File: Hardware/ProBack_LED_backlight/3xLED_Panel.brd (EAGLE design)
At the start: 48 x 6 mm, 11 parts

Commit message: Update boards and schematic
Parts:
- moved D1 0.05 mm to (12.0, 1.30), turned to 180 degrees
- turned D2 to 180 degrees
- turned D3 to 180 degrees
- turned D4 to 180 degrees
- turned D5 to 180 degrees
- turned D6 to 180 degrees
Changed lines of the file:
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@@
 </autorouter>
 <elements>
-<element name="D1" library="Yuji_LED" package="2835_SMD" value="YUJI_2835_SMD" x="12" y="1.25" smashed="yes">
-<attribute name="NAME" x="14.62" y="0.92" size="0.6096" layer="21"/>
-</element>
-<element name="D2" library="Yuji_LED" package="2835_SMD" value="YUJI_2835_SMD" x="24" y="1.25" smashed="yes">
-<attribute name="NAME" x="26.62" y="1.02" size="0.6096" layer="21"/>
+<element name="D1" library="Yuji_LED" package="2835_SMD" value="YUJI_2835_SMD" x="12" y="1.3" smashed="yes" rot="R180"/>
+<element name="D2" library="Yuji_LED" package="2835_SMD" value="YUJI_2835_SMD" x="24" y="1.25" smashed="yes" rot="R180">
+<attribute name="NAME" x="21.38" y="1.48" size="0.6096" layer="21" rot="R180"/>
 </element>
 <element name="FRAME1" library="SparkFun-Aesthetics" package="CREATIVE_COMMONS" value="FRAME-LEDGER" x="0" y="0" smashed="yes">
@@
 <attribute name="VALUE" x="46.1" y="1.3" size="0.0254" layer="27" rot="R90"/>
 </element>
-<element name="D3" library="Yuji_LED" package="2835_SMD" value="YUJI_2835_SMD" x="36" y="1.25" smashed="yes">
-<attribute name="NAME" x="38.52" y="1.02" size="0.6096" layer="21"/>
+<element name="D3" library="Yuji_LED" package="2835_SMD" value="YUJI_2835_SMD" x="36" y="1.25" smashed="yes" rot="R180">
+<attribute name="NAME" x="33.48" y="1.48" size="0.6096" layer="21" rot="R180"/>
 </element>
-<element name="D4" library="Yuji_LED" package="2835_SMD" value="YUJI_2835_SMD" x="12" y="4.75" smashed="yes"/>
-<element name="D5" library="Yuji_LED" package="2835_SMD" value="YUJI_2835_SMD" x="24" y="4.75" smashed="yes"/>
+<element name="D4" library="Yuji_LED" package="2835_SMD" value="YUJI_2835_SMD" x="12" y="4.75" smashed="yes" rot="R180"/>
+<element name="D5" library="Yuji_LED" package="2835_SMD" value="YUJI_2835_SMD" x="24" y="4.75" smashed="yes" rot="R180"/>
 <element name="+1" library="wirepad" package="2,15/1,0" package3d_urn="urn:adsk.eagle:package:30831/1" value="WIREPAD1,6/0,9" x="1.9" y="4.7" smashed="yes">
 <attribute name="POPULARITY" value="11" x="1.9" y="-3.3" size="1.778" layer="27" display="off"/>
@@
 <attribute name="VALUE" x="46.1" y="5.7" size="0.0254" layer="27"/>
 </element>
-<element name="D6" library="Yuji_LED" package="2835_SMD" value="YUJI_2835_SMD" x="36" y="4.75" smashed="yes"/>
+<element name="D6" library="Yuji_LED" package="2835_SMD" value="YUJI_2835_SMD" x="36" y="4.75" smashed="yes" rot="R180"/>
 </elements>
 <signals>
@@
 <contactref element="D1" pad="CATHODE"/>
 <contactref element="D2" pad="ANODE"/>
-<wire x1="12.95" y1="1.25" x2="22.7" y2="1.25" width="1.27" layer="1"/>
+<wire x1="13.3" y1="1.3" x2="23.05" y2="1.25" width="1.27" layer="1"/>
 </signal>
 <signal name="N$2">
 <contactref element="+" pad="1"/>
 <contactref element="D1" pad="ANODE"/>
-<wire x1="1.9" y1="1.3" x2="10.65" y2="1.3" width="1.27" layer="1"/>
-<wire x1="10.65" y1="1.3" x2="10.7" y2="1.25" width="1.27" layer="1"/>
+<wire x1="1.9" y1="1.3" x2="11.05" y2="1.3" width="1.27" layer="1"/>
 </signal>
 <signal name="N$3">
 <contactref element="D2" pad="CATHODE"/>
 <contactref element="D3" pad="ANODE"/>
-<wire x1="24.95" y1="1.25" x2="34.7" y2="1.25" width="1.27" layer="1"/>
+<wire x1="35.05" y1="1.25" x2="25.3" y2="1.25" width="1.27" layer="1"/>
 </signal>
 <signal name="N$4">
 <contactref element="D3" pad="CATHODE"/>
 <contactref element="-" pad="1"/>
-<wire x1="36.95" y1="1.25" x2="46.05" y2="1.25" width="1.27" layer="1"/>
+<wire x1="37.3" y1="1.25" x2="46.05" y2="1.25" width="1.27" layer="1"/>
 <wire x1="46.05" y1="1.25" x2="46.1" y2="1.3" width="1.27" layer="1"/>
 </signal>
@@
 <contactref element="D4" pad="CATHODE"/>
 <contactref element="D5" pad="ANODE"/>
-<wire x1="12.95" y1="4.75" x2="22.7" y2="4.75" width="1.27" layer="1"/>
+<wire x1="13.3" y1="4.75" x2="23.05" y2="4.75" width="1.27" layer="1"/>
 </signal>
 <signal name="N$6">
@@
 <contactref element="D4" pad="ANODE"/>
 <wire x1="1.9" y1="4.7" x2="1.95" y2="4.75" width="1.27" layer="1"/>
-<wire x1="1.95" y1="4.75" x2="10.7" y2="4.75" width="1.27" layer="1"/>
+<wire x1="1.95" y1="4.75" x2="11.05" y2="4.75" width="1.27" layer="1"/>
 </signal>
 <signal name="N$7">
 <contactref element="D5" pad="CATHODE"/>
 <contactref element="D6" pad="ANODE"/>
-<wire x1="24.95" y1="4.75" x2="34.7" y2="4.75" width="1.27" layer="1"/>
+<wire x1="25.3" y1="4.75" x2="35.05" y2="4.75" width="1.27" layer="1"/>
 </signal>
 <signal name="N$8">
 <contactref element="D6" pad="CATHODE"/>
 <contactref element="-1" pad="1"/>
-<wire x1="36.95" y1="4.75" x2="46.05" y2="4.75" width="1.27" layer="1"/>
+<wire x1="37.3" y1="4.75" x2="46.05" y2="4.75" width="1.27" layer="1"/>
 <wire x1="46.05" y1="4.75" x2="46.1" y2="4.7" width="1.27" layer="1"/>
 </signal>

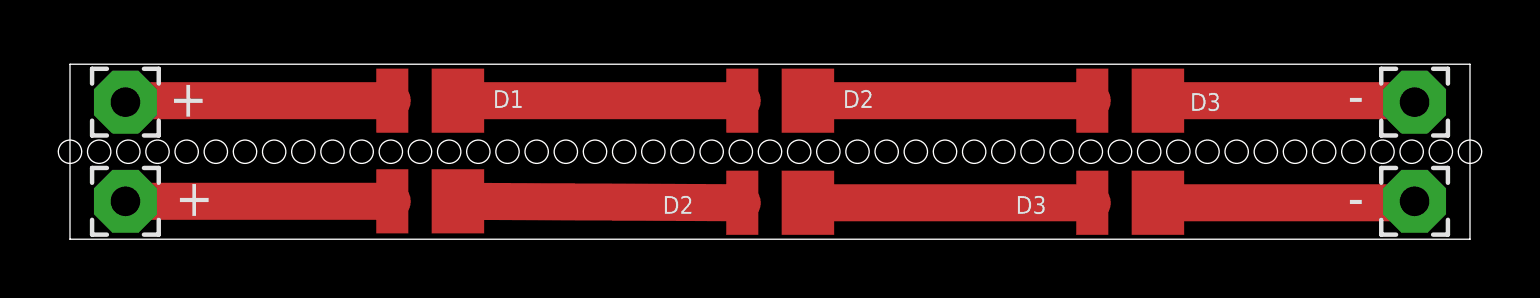
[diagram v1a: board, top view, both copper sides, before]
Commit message: Updated for PCBWay of doing boards
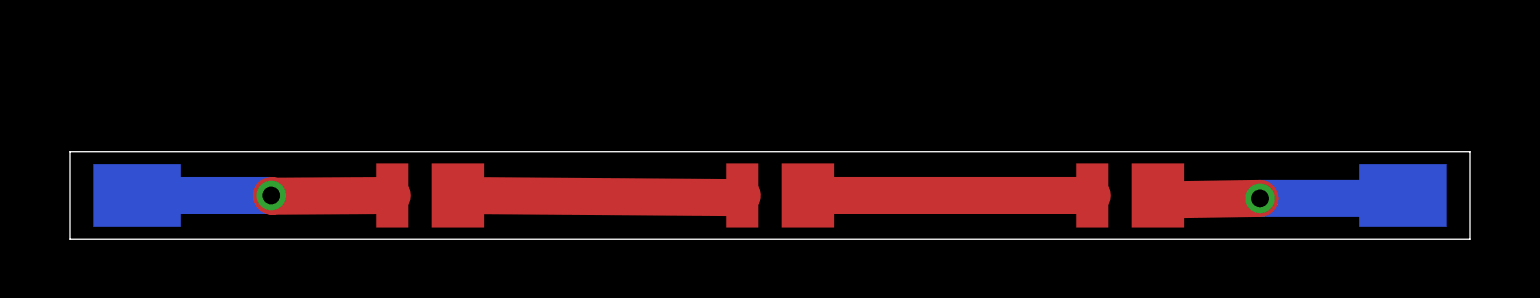
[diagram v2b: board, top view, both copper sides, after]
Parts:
- removed +1: WIREPAD1,6/0,9, wirepad:2,15/1,0
- removed -1: (no value), wirepad:2,15/1,0
- removed D4, D5, D6: YUJI_2835_SMD, Yuji_LED:2835_SMD
- +, -: device wirepad:2,15/1,0 -> wirepad:SMD3-2,15
- moved + 0.45 mm to (2.30, 1.50), flipped to the bottom, turned to 0 degrees
- moved - 0.45 mm to (45.7, 1.50), flipped to the bottom, turned to 0 degrees
- moved D2 0.25 mm to (24.0, 1.50)
- moved D3 0.25 mm to (36.0, 1.50)
- moved D1 0.20 mm to (12.0, 1.50)
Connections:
- removed net N$5: D4.CATHODE, D5.ANODE
- removed net N$6: +1.1, D4.ANODE
- removed net N$7: D5.CATHODE, D6.ANODE
- removed net N$8: -1.1, D6.CATHODE
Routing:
- net N$5: track 9.75 -> 0.00 mm
- net N$7: track 9.75 -> 0.00 mm
- net N$6: track 9.17 -> 0.00 mm
- net N$8: track 8.82 -> 0.00 mm
- net N$2: track 9.15 -> 8.76 mm, vias 0 -> 1
- net N$4: track 8.82 -> 8.89 mm, vias 0 -> 1
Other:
- board size 48 x 6 mm -> 48 x 3 mm
- board text removed: "- LED"
- board text removed: "-LED"
- board text removed: "D1"
- board text removed: "D2"
- board text removed: "D3"
- board text removed: "LED +"
- board text removed: "LED+"
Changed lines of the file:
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@@
 <setting verticaltext="up"/>
 </settings>
-<grid distance="1" unitdist="mm" unit="mm" style="lines" multiple="1" display="yes" altdistance="0.1" altunitdist="mm" altunit="mm"/>
+<grid distance="1" unitdist="mm" unit="mm" style="lines" multiple="1" display="yes" altdistance="0.05" altunitdist="mm" altunit="mm"/>
 <layers>
 <layer number="1" name="Top" color="4" fill="1" visible="yes" active="yes"/>
@@
 <plain>
 <wire x1="0" y1="0" x2="48" y2="0" width="0" layer="20"/>
-<wire x1="48" y1="0" x2="48" y2="6" width="0" layer="20"/>
-<wire x1="48" y1="6" x2="0" y2="6" width="0" layer="20"/>
-<wire x1="0" y1="6" x2="0" y2="0" width="0" layer="20"/>
-<text x="7.1" y="0.8" size="1.016" layer="26" rot="MR0">LED +</text>
-<text x="44.8" y="0.8" size="1.016" layer="26" rot="MR0">- LED</text>
-<text x="14.5" y="4.5" size="0.6096" layer="25">D1</text>
-<text x="26.5" y="4.5" size="0.6096" layer="25">D2</text>
-<text x="38.4" y="4.4" size="0.6096" layer="25">D3</text>
-<text x="3.4" y="4.2" size="1.27" layer="25">+</text>
-<text x="43.8" y="4.3" size="1.27" layer="25">-</text>
-<text x="6.7" y="4.3" size="1.016" layer="26" rot="MR0">LED+</text>
-<text x="44.7" y="4.3" size="1.016" layer="26" rot="MR0">-LED</text>
-<hole x="48" y="3" drill="0.8"/>
-<hole x="47" y="3" drill="0.8"/>
-<hole x="46" y="3" drill="0.8"/>
-<hole x="45" y="3" drill="0.8"/>
-<hole x="44" y="3" drill="0.8"/>
-<hole x="43" y="3" drill="0.8"/>
-<hole x="42" y="3" drill="0.8"/>
-<hole x="41" y="3" drill="0.8"/>
-<hole x="40" y="3" drill="0.8"/>
-<hole x="39" y="3" drill="0.8"/>
-<hole x="38" y="3" drill="0.8"/>
-<hole x="37" y="3" drill="0.8"/>
-<hole x="36" y="3" drill="0.8"/>
-<hole x="35" y="3" drill="0.8"/>
-<hole x="34" y="3" drill="0.8"/>
-<hole x="33" y="3" drill="0.8"/>
-<hole x="32" y="3" drill="0.8"/>
-<hole x="31" y="3" drill="0.8"/>
-<hole x="30" y="3" drill="0.8"/>
-<hole x="29" y="3" drill="0.8"/>
-<hole x="28" y="3" drill="0.8"/>
-<hole x="27" y="3" drill="0.8"/>
-<hole x="26" y="3" drill="0.8"/>
-<hole x="25" y="3" drill="0.8"/>
-<hole x="24" y="3" drill="0.8"/>
-<hole x="23" y="3" drill="0.8"/>
-<hole x="22" y="3" drill="0.8"/>
-<hole x="21" y="3" drill="0.8"/>
-<hole x="20" y="3" drill="0.8"/>
-<hole x="19" y="3" drill="0.8"/>
-<hole x="18" y="3" drill="0.8"/>
-<hole x="17" y="3" drill="0.8"/>
-<hole x="16" y="3" drill="0.8"/>
-<hole x="15" y="3" drill="0.8"/>
-<hole x="14" y="3" drill="0.8"/>
-<hole x="13" y="3" drill="0.8"/>
-<hole x="12" y="3" drill="0.8"/>
-<hole x="11" y="3" drill="0.8"/>
-<hole x="10" y="3" drill="0.8"/>
-<hole x="9" y="3" drill="0.8"/>
-<hole x="8" y="3" drill="0.8"/>
-<hole x="7" y="3" drill="0.8"/>
-<hole x="6" y="3" drill="0.8"/>
-<hole x="5" y="3" drill="0.8"/>
-<hole x="4" y="3" drill="0.8"/>
-<hole x="3" y="3" drill="0.8"/>
-<hole x="2" y="3" drill="0.8"/>
-<hole x="1" y="3" drill="0.8"/>
-<hole x="0" y="3" drill="0.8"/>
+<wire x1="48" y1="0" x2="48" y2="3" width="0" layer="20"/>
+<wire x1="48" y1="3" x2="0" y2="3" width="0" layer="20"/>
+<wire x1="0" y1="3" x2="0" y2="0" width="0" layer="20"/>
+<text x="6.2" y="0.2" size="2.54" layer="26" rot="MR0">+</text>
+<text x="43.6" y="0.5" size="2.54" layer="26" rot="MR0">-</text>
 </plain>
 <attributes>
@@
 </autorouter>
 <elements>
-<element name="D1" library="Yuji_LED" package="2835_SMD" value="YUJI_2835_SMD" x="12" y="1.3" smashed="yes" rot="R180"/>
-<element name="D2" library="Yuji_LED" package="2835_SMD" value="YUJI_2835_SMD" x="24" y="1.25" smashed="yes" rot="R180">
-<attribute name="NAME" x="21.38" y="1.48" size="0.6096" layer="21" rot="R180"/>
-</element>
+<element name="D1" library="Yuji_LED" package="2835_SMD" value="YUJI_2835_SMD" x="12" y="1.5" smashed="yes" rot="R180"/>
+<element name="D2" library="Yuji_LED" package="2835_SMD" value="YUJI_2835_SMD" x="24" y="1.5" smashed="yes" rot="R180"/>
 <element name="FRAME1" library="SparkFun-Aesthetics" package="CREATIVE_COMMONS" value="FRAME-LEDGER" x="0" y="0" smashed="yes">
 <attribute name="AUTHOR" value="Alexey Danilchenko" x="0" y="0" size="1.778" layer="27" display="off"/>
 <attribute name="VER" value="1.0" x="0" y="0" size="1.778" layer="27" display="off"/>
 </element>
-<element name="+" library="wirepad" package="2,15/1,0" package3d_urn="urn:adsk.eagle:package:30831/1" value="WIREPAD1,6/0,9" x="1.9" y="1.3" smashed="yes" rot="R270">
-<attribute name="NAME" x="3.6" y="0.8" size="1.27" layer="25"/>
-<attribute name="POPULARITY" value="11" x="1.9" y="1.3" size="1.778" layer="27" rot="R270" display="off"/>
-<attribute name="VALUE" x="1.9" y="1.3" size="0.0254" layer="27" rot="R270"/>
+<element name="+" library="wirepad" package="SMD3-2,15" value="WIREPAD1,6/0,9" x="2.3" y="1.5" smashed="yes" rot="MR0">
+<attribute name="VALUE" x="2.3" y="1.5" size="0.0254" layer="28" rot="MR0"/>
 </element>
-<element name="-" library="wirepad" package="2,15/1,0" package3d_urn="urn:adsk.eagle:package:30831/1" value="" x="46.1" y="1.3" smashed="yes" rot="R90">
-<attribute name="NAME" x="43.8" y="0.8" size="1.27" layer="25"/>
-<attribute name="POPULARITY" value="11" x="46.1" y="1.3" size="1.778" layer="27" rot="R90" display="off"/>
-<attribute name="VALUE" x="46.1" y="1.3" size="0.0254" layer="27" rot="R90"/>
+<element name="-" library="wirepad" package="SMD3-2,15" value="" x="45.7" y="1.5" smashed="yes" rot="MR0">
+<attribute name="VALUE" x="45.7" y="1.5" size="0.0254" layer="28" rot="MR0"/>
 </element>
-<element name="D3" library="Yuji_LED" package="2835_SMD" value="YUJI_2835_SMD" x="36" y="1.25" smashed="yes" rot="R180">
-<attribute name="NAME" x="33.48" y="1.48" size="0.6096" layer="21" rot="R180"/>
-</element>
-<element name="D4" library="Yuji_LED" package="2835_SMD" value="YUJI_2835_SMD" x="12" y="4.75" smashed="yes" rot="R180"/>
-<element name="D5" library="Yuji_LED" package="2835_SMD" value="YUJI_2835_SMD" x="24" y="4.75" smashed="yes" rot="R180"/>
-<element name="+1" library="wirepad" package="2,15/1,0" package3d_urn="urn:adsk.eagle:package:30831/1" value="WIREPAD1,6/0,9" x="1.9" y="4.7" smashed="yes">
-<attribute name="POPULARITY" value="11" x="1.9" y="-3.3" size="1.778" layer="27" display="off"/>
-<attribute name="VALUE" x="1.9" y="5.7" size="0.0254" layer="27"/>
-</element>
-<element name="-1" library="wirepad" package="2,15/1,0" package3d_urn="urn:adsk.eagle:package:30831/1" value="" x="46.1" y="4.7" smashed="yes">
-<attribute name="POPULARITY" value="11" x="42.1" y="-8.3" size="1.778" layer="27" display="off"/>
-<attribute name="VALUE" x="46.1" y="5.7" size="0.0254" layer="27"/>
-</element>
-<element name="D6" library="Yuji_LED" package="2835_SMD" value="YUJI_2835_SMD" x="36" y="4.75" smashed="yes" rot="R180"/>
+<element name="D3" library="Yuji_LED" package="2835_SMD" value="YUJI_2835_SMD" x="36" y="1.5" smashed="yes" rot="R180"/>
 </elements>
 <signals>
@@
 <contactref element="D1" pad="CATHODE"/>
 <contactref element="D2" pad="ANODE"/>
-<wire x1="13.3" y1="1.3" x2="23.05" y2="1.25" width="1.27" layer="1"/>
+<wire x1="22.99923125" y1="1.4252625" x2="13.3" y2="1.5" width="1.27" layer="1"/>
+<wire x1="22.99923125" y1="1.4252625" x2="23.05" y2="1.5" width="1.27" layer="1"/>
 </signal>
 <signal name="N$2">
 <contactref element="+" pad="1"/>
 <contactref element="D1" pad="ANODE"/>
-<wire x1="1.9" y1="1.3" x2="11.05" y2="1.3" width="1.27" layer="1"/>
+<wire x1="6.9" y1="1.5" x2="2.3" y2="1.5" width="1.27" layer="16"/>
+<via x="6.9" y="1.5" extent="1-16" drill="0.6096"/>
+<wire x1="6.9" y1="1.5" x2="6.925" y2="1.475" width="1.27" layer="1"/>
+<wire x1="11.05" y1="1.5" x2="6.925" y2="1.475" width="1.27" layer="1"/>
 </signal>
 <signal name="N$3">
 <contactref element="D2" pad="CATHODE"/>
 <contactref element="D3" pad="ANODE"/>
-<wire x1="35.05" y1="1.25" x2="25.3" y2="1.25" width="1.27" layer="1"/>
+<wire x1="35.05" y1="1.5" x2="25.3" y2="1.5" width="1.27" layer="1"/>
 </signal>
 <signal name="N$4">
 <contactref element="D3" pad="CATHODE"/>
 <contactref element="-" pad="1"/>
-<wire x1="37.3" y1="1.25" x2="46.05" y2="1.25" width="1.27" layer="1"/>
-<wire x1="46.05" y1="1.25" x2="46.1" y2="1.3" width="1.27" layer="1"/>
-</signal>
-<signal name="N$5">
-<contactref element="D4" pad="CATHODE"/>
-<contactref element="D5" pad="ANODE"/>
-<wire x1="13.3" y1="4.75" x2="23.05" y2="4.75" width="1.27" layer="1"/>
-</signal>
-<signal name="N$6">
-<contactref element="+1" pad="1"/>
-<contactref element="D4" pad="ANODE"/>
-<wire x1="1.9" y1="4.7" x2="1.95" y2="4.75" width="1.27" layer="1"/>
-<wire x1="1.95" y1="4.75" x2="11.05" y2="4.75" width="1.27" layer="1"/>
-</signal>
-<signal name="N$7">
-<contactref element="D5" pad="CATHODE"/>
-<contactref element="D6" pad="ANODE"/>
-<wire x1="25.3" y1="4.75" x2="35.05" y2="4.75" width="1.27" layer="1"/>
-</signal>
-<signal name="N$8">
-<contactref element="D6" pad="CATHODE"/>
-<contactref element="-1" pad="1"/>
-<wire x1="37.3" y1="4.75" x2="46.05" y2="4.75" width="1.27" layer="1"/>
-<wire x1="46.05" y1="4.75" x2="46.1" y2="4.7" width="1.27" layer="1"/>
+<wire x1="45.9" y1="1.4" x2="40.8" y2="1.4" width="1.27" layer="16"/>
+<wire x1="45.7" y1="1.5" x2="45.9" y2="1.4" width="1.27" layer="16"/>
+<via x="40.8" y="1.4" extent="1-16" drill="0.6096"/>
+<wire x1="40.8" y1="1.4" x2="37.435796875" y2="1.347434375" width="1.27" layer="1"/>
+<wire x1="37.435796875" y1="1.347434375" x2="37.3" y2="1.5" width="1.27" layer="1"/>
 </signal>
 </signals>
@@
 </board>
 </drawing>
-<compatibility>
-<note version="8.3" severity="warning">
-Since Version 8.3, EAGLE supports URNs for individual library
-assets (packages, symbols, and devices). The URNs of those assets
-will not be understood (or retained) with this version.
-</note>
-<note version="8.3" severity="warning">
-Since Version 8.3, EAGLE supports the association of 3D packages
-with devices in libraries, schematics, and board files. Those 3D
-packages will not be understood (or retained) with this version.
-</note>
-</compatibility>
 </eagle>
